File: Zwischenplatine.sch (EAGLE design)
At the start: 7 parts

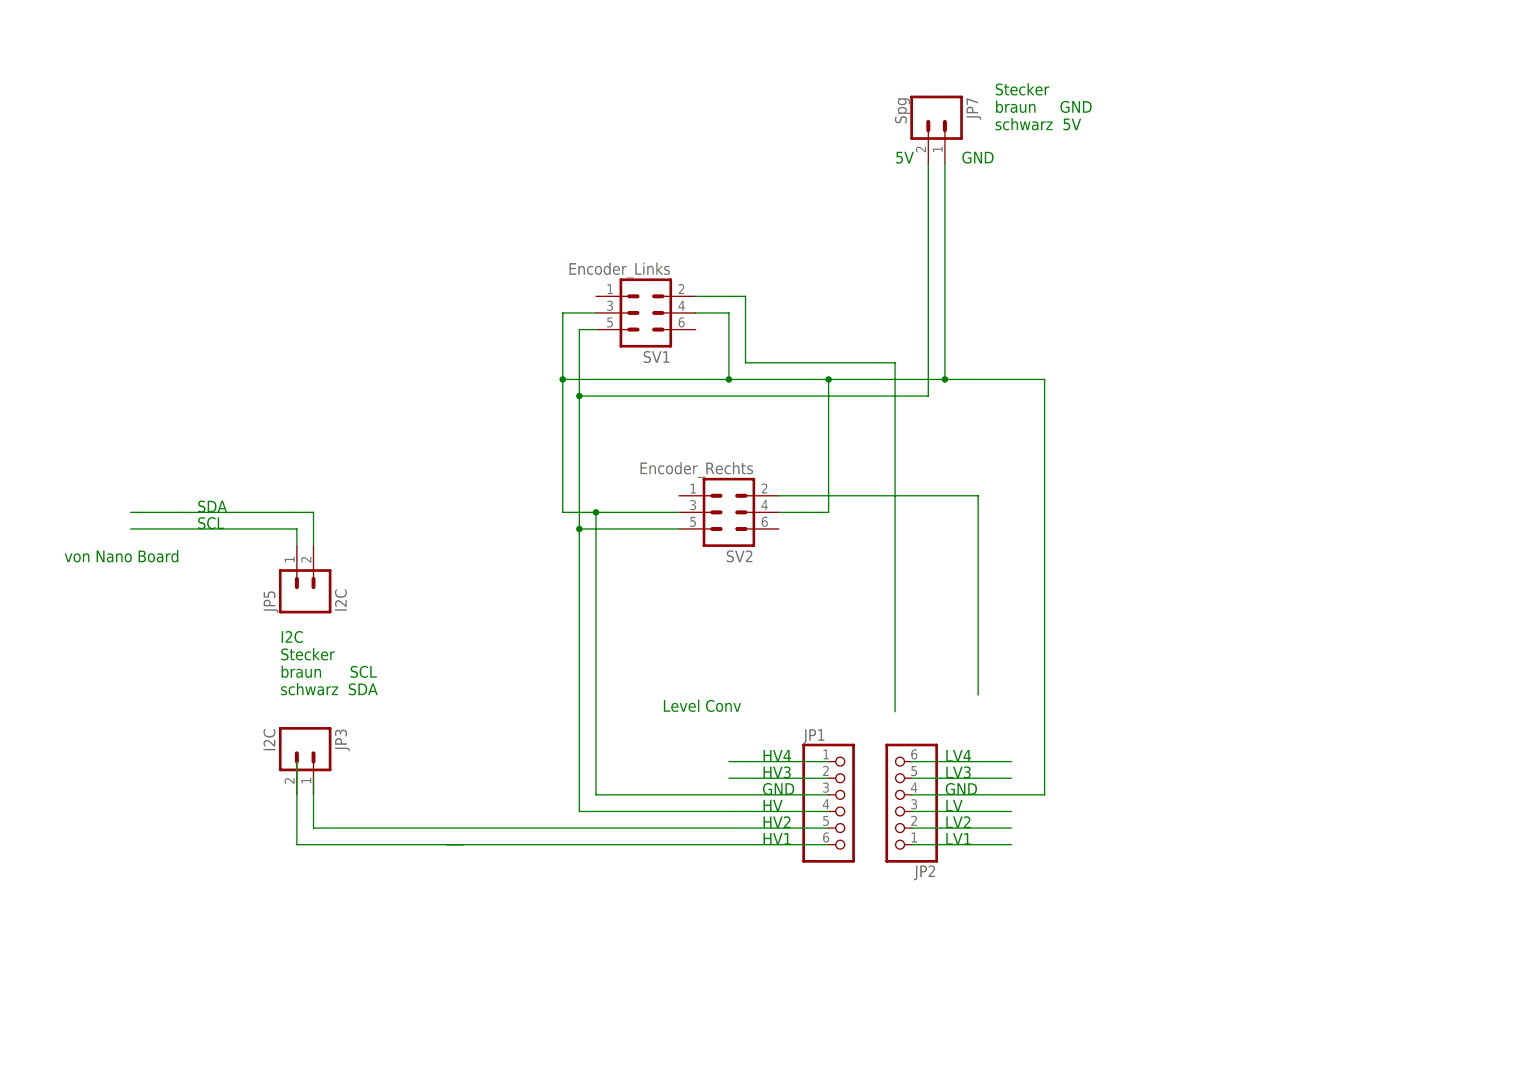
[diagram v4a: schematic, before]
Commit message: 
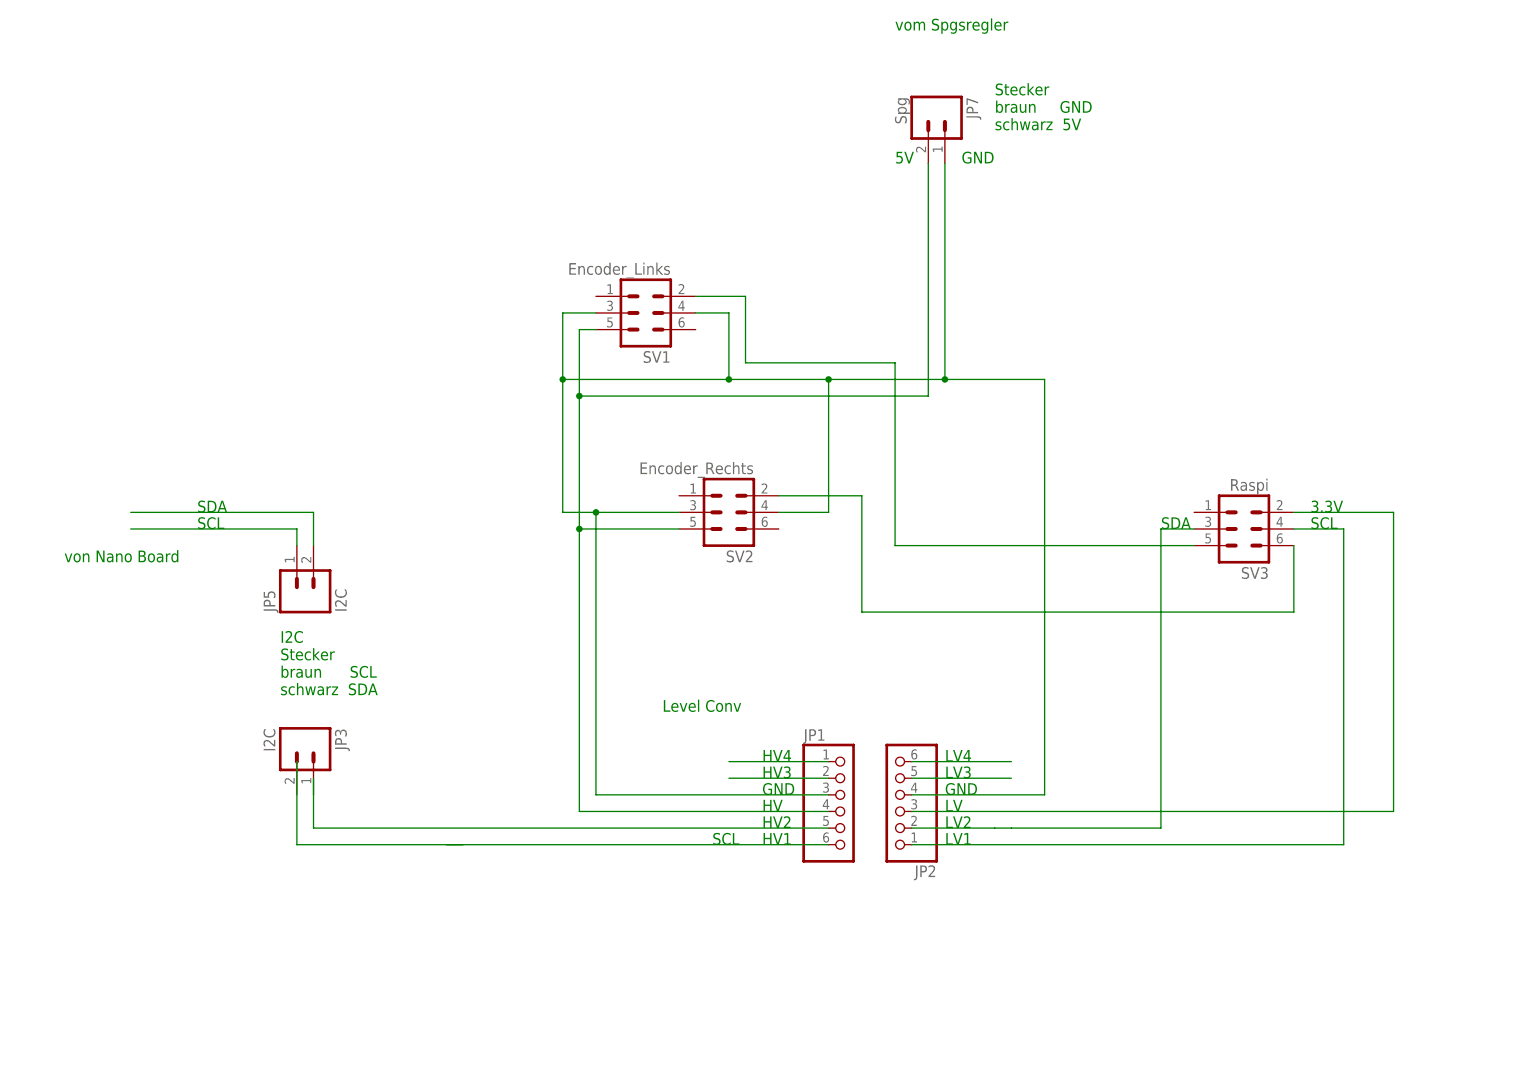
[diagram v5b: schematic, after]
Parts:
- added SV3: Raspi, con-ml:ML6
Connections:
- net N$12: now also SV3.2
- net N$13: now also SV3.3
- net N$14: now also SV3.4
- net PE4: now also SV3.5
- net PE5: now also SV3.6
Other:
- note added: "3.3V"
- note added: "vom Spgsregler"
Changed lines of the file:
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@@
 <part name="JP5" library="SparkFun-Connectors" deviceset="M02" device="-JST-2MM-SMT" value="I2C"/>
 <part name="JP3" library="SparkFun-Connectors" deviceset="M02" device="-JST-2MM-SMT" value="I2C"/>
+<part name="SV3" library="con-ml" deviceset="ML6" device="" value="Raspi"/>
 </parts>
 <sheets>
@@
 schwarz  SDA</text>
 <text x="-73.66" y="78.74" size="1.778" layer="91">von Nano Board</text>
+<text x="25.4" y="35.56" size="1.778" layer="91">SCL</text>
+<text x="116.84" y="83.82" size="1.778" layer="91">SCL</text>
+<text x="116.84" y="86.36" size="1.778" layer="91">3.3V</text>
+<text x="93.98" y="83.82" size="1.778" layer="91">SDA</text>
+<text x="53.34" y="160.02" size="1.778" layer="91">vom Spgsregler</text>
 </plain>
 <instances>
@@
 <instance part="JP5" gate="G$1" x="-35.56" y="73.66" rot="R90"/>
 <instance part="JP3" gate="G$1" x="-38.1" y="50.8" rot="R270"/>
+<instance part="SV3" gate="1" x="106.68" y="83.82" smashed="yes" rot="R180">
+<attribute name="VALUE" x="110.49" y="91.44" size="1.778" layer="96" rot="R180"/>
+<attribute name="NAME" x="110.49" y="77.978" size="1.778" layer="95" rot="R180"/>
+</instance>
 </instances>
 <busses>
@@
 <net name="PE5" class="0">
 <segment>
-<wire x1="35.56" y1="88.9" x2="66.04" y2="88.9" width="0.1524" layer="91"/>
-<wire x1="66.04" y1="88.9" x2="66.04" y2="58.42" width="0.1524" layer="91"/>
+<pinref part="SV3" gate="1" pin="6"/>
+<wire x1="114.3" y1="81.28" x2="114.3" y2="71.12" width="0.1524" layer="91"/>
+<wire x1="114.3" y1="71.12" x2="48.26" y2="71.12" width="0.1524" layer="91"/>
 <pinref part="SV2" gate="1" pin="2"/>
+<wire x1="35.56" y1="88.9" x2="48.26" y2="88.9" width="0.1524" layer="91"/>
+<wire x1="48.26" y1="88.9" x2="48.26" y2="71.12" width="0.1524" layer="91"/>
 </segment>
 </net>
@@
 <wire x1="30.48" y1="119.38" x2="30.48" y2="109.22" width="0.1524" layer="91"/>
 <wire x1="30.48" y1="109.22" x2="53.34" y2="109.22" width="0.1524" layer="91"/>
-<wire x1="53.34" y1="109.22" x2="53.34" y2="55.88" width="0.1524" layer="91"/>
+<wire x1="53.34" y1="109.22" x2="53.34" y2="81.28" width="0.1524" layer="91"/>
 <pinref part="SV1" gate="1" pin="2"/>
 <wire x1="30.48" y1="119.38" x2="22.86" y2="119.38" width="0.1524" layer="91"/>
+<pinref part="SV3" gate="1" pin="5"/>
+<wire x1="99.06" y1="81.28" x2="53.34" y2="81.28" width="0.1524" layer="91"/>
 </segment>
 </net>
@@
 <wire x1="5.08" y1="83.82" x2="5.08" y2="40.64" width="0.1524" layer="91"/>
 <pinref part="JP1" gate="A" pin="4"/>
-<wire x1="43.18" y1="40.64" x2="30.48" y2="40.64" width="0.1524" layer="91"/>
-<wire x1="30.48" y1="40.64" x2="27.94" y2="40.64" width="0.1524" layer="91"/>
-<wire x1="5.08" y1="40.64" x2="27.94" y2="40.64" width="0.1524" layer="91"/>
+<wire x1="5.08" y1="40.64" x2="43.18" y2="40.64" width="0.1524" layer="91"/>
 <junction x="5.08" y="83.82"/>
 </segment>
@@
 <segment>
 <pinref part="JP2" gate="A" pin="3"/>
-<wire x1="55.88" y1="40.64" x2="71.12" y2="40.64" width="0.1524" layer="91"/>
+<wire x1="55.88" y1="40.64" x2="129.54" y2="40.64" width="0.1524" layer="91"/>
+<wire x1="129.54" y1="40.64" x2="129.54" y2="86.36" width="0.1524" layer="91"/>
+<pinref part="SV3" gate="1" pin="2"/>
+<wire x1="129.54" y1="86.36" x2="114.3" y2="86.36" width="0.1524" layer="91"/>
 </segment>
 </net>
@@
 <segment>
 <pinref part="JP2" gate="A" pin="2"/>
-<wire x1="55.88" y1="38.1" x2="71.12" y2="38.1" width="0.1524" layer="91"/>
+<wire x1="55.88" y1="38.1" x2="68.58" y2="38.1" width="0.1524" layer="91"/>
+<pinref part="SV3" gate="1" pin="3"/>
+<wire x1="68.58" y1="38.1" x2="71.12" y2="38.1" width="0.1524" layer="91"/>
+<wire x1="99.06" y1="83.82" x2="93.98" y2="83.82" width="0.1524" layer="91"/>
+<wire x1="93.98" y1="83.82" x2="93.98" y2="38.1" width="0.1524" layer="91"/>
+<wire x1="93.98" y1="38.1" x2="71.12" y2="38.1" width="0.1524" layer="91"/>
 </segment>
 </net>
@@
 <segment>
 <pinref part="JP2" gate="A" pin="1"/>
-<wire x1="55.88" y1="35.56" x2="71.12" y2="35.56" width="0.1524" layer="91"/>
-</segment>
-</net>
+<wire x1="55.88" y1="35.56" x2="121.92" y2="35.56" width="0.1524" layer="91"/>
+<wire x1="121.92" y1="35.56" x2="121.92" y2="83.82" width="0.1524" layer="91"/>
+<pinref part="SV3" gate="1" pin="4"/>
+<wire x1="121.92" y1="83.82" x2="114.3" y2="83.82" width="0.1524" layer="91"/>
+</segment>
+</net>

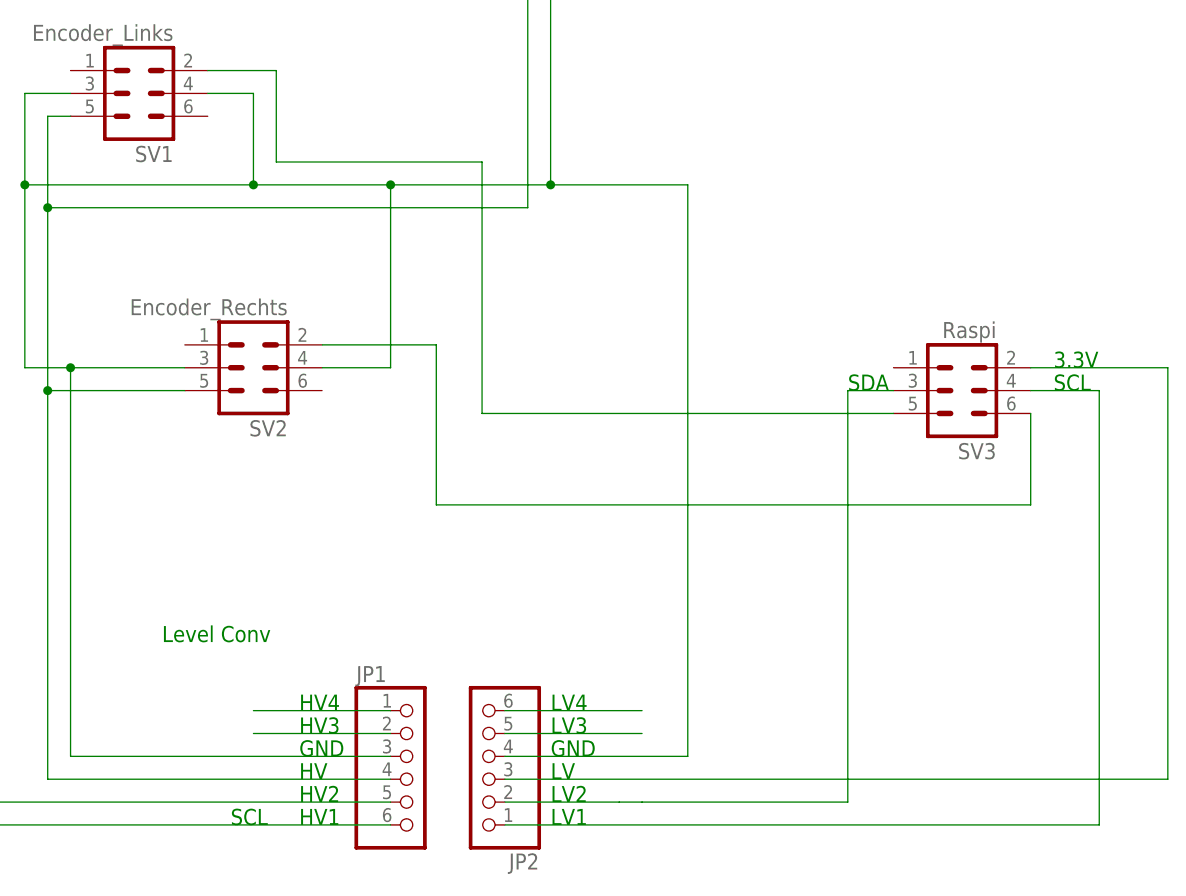
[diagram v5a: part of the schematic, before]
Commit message: 
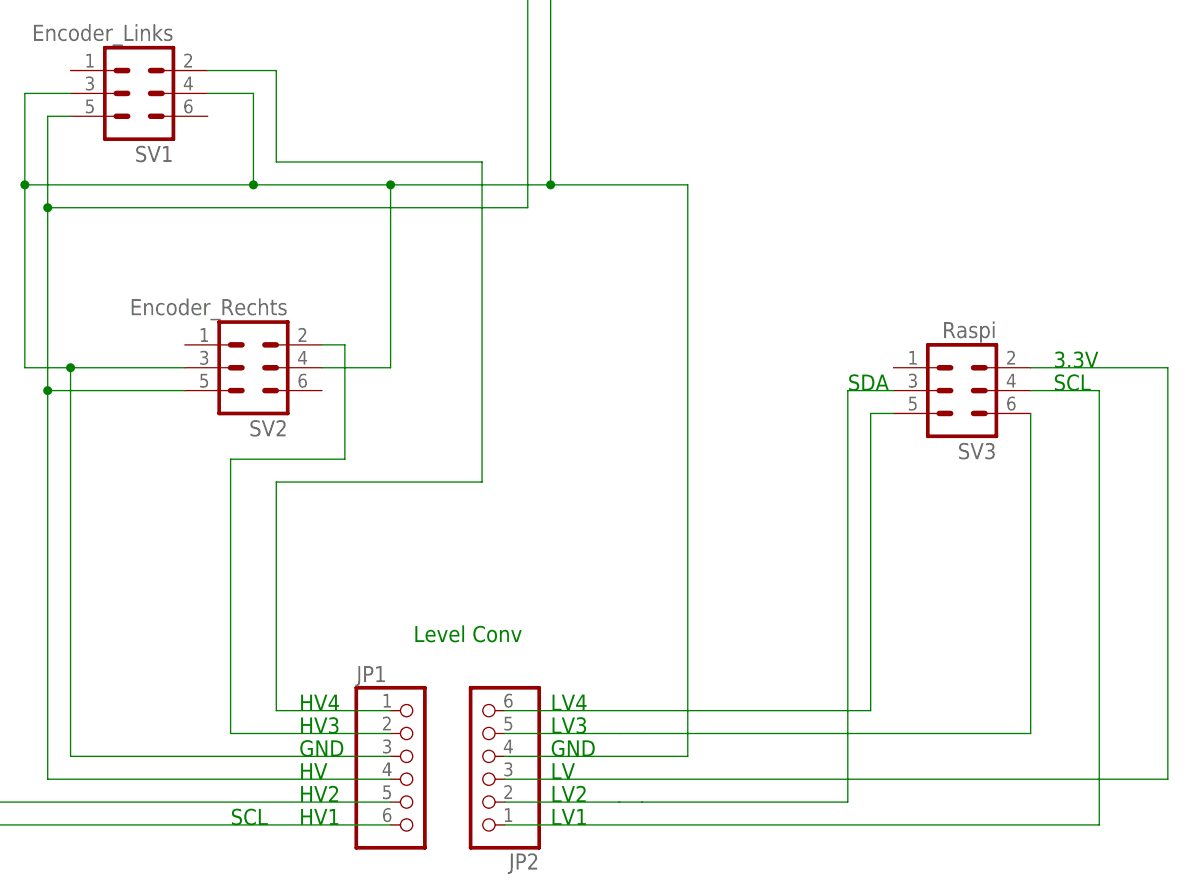
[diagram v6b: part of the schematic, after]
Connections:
- removed net N$3: JP1.1
- removed net N$4: JP1.2
- net N$10: now also SV3.6
- net N$9: now also SV3.5
- net PE4: now also JP1.1; no longer SV3.5
- net PE5: now also JP1.2; no longer SV3.6
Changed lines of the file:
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@@
 braun     GND
 schwarz  5V</text>
-<text x="17.78" y="55.88" size="1.778" layer="91">Level Conv</text>
+<text x="45.72" y="55.88" size="1.778" layer="91">Level Conv</text>
 <text x="33.02" y="35.56" size="1.778" layer="91">HV1</text>
 <text x="33.02" y="38.1" size="1.778" layer="91">HV2</text>
@@
 <net name="PE5" class="0">
 <segment>
-<pinref part="SV3" gate="1" pin="6"/>
-<wire x1="114.3" y1="81.28" x2="114.3" y2="71.12" width="0.1524" layer="91"/>
-<wire x1="114.3" y1="71.12" x2="48.26" y2="71.12" width="0.1524" layer="91"/>
 <pinref part="SV2" gate="1" pin="2"/>
-<wire x1="35.56" y1="88.9" x2="48.26" y2="88.9" width="0.1524" layer="91"/>
-<wire x1="48.26" y1="88.9" x2="48.26" y2="71.12" width="0.1524" layer="91"/>
+<wire x1="35.56" y1="88.9" x2="38.1" y2="88.9" width="0.1524" layer="91"/>
+<pinref part="JP1" gate="A" pin="2"/>
+<wire x1="43.18" y1="45.72" x2="25.4" y2="45.72" width="0.1524" layer="91"/>
+<wire x1="25.4" y1="45.72" x2="25.4" y2="76.2" width="0.1524" layer="91"/>
+<wire x1="25.4" y1="76.2" x2="38.1" y2="76.2" width="0.1524" layer="91"/>
+<wire x1="38.1" y1="76.2" x2="38.1" y2="88.9" width="0.1524" layer="91"/>
 </segment>
 </net>
@@
 <wire x1="30.48" y1="119.38" x2="30.48" y2="109.22" width="0.1524" layer="91"/>
 <wire x1="30.48" y1="109.22" x2="53.34" y2="109.22" width="0.1524" layer="91"/>
-<wire x1="53.34" y1="109.22" x2="53.34" y2="81.28" width="0.1524" layer="91"/>
+<wire x1="53.34" y1="109.22" x2="53.34" y2="73.66" width="0.1524" layer="91"/>
 <pinref part="SV1" gate="1" pin="2"/>
 <wire x1="30.48" y1="119.38" x2="22.86" y2="119.38" width="0.1524" layer="91"/>
-<pinref part="SV3" gate="1" pin="5"/>
-<wire x1="99.06" y1="81.28" x2="53.34" y2="81.28" width="0.1524" layer="91"/>
+<pinref part="JP1" gate="A" pin="1"/>
+<wire x1="43.18" y1="48.26" x2="30.48" y2="48.26" width="0.1524" layer="91"/>
+<wire x1="30.48" y1="48.26" x2="30.48" y2="73.66" width="0.1524" layer="91"/>
+<wire x1="30.48" y1="73.66" x2="53.34" y2="73.66" width="0.1524" layer="91"/>
 </segment>
 </net>
@@
 </segment>
 </net>
-<net name="N$3" class="0">
-<segment>
-<pinref part="JP1" gate="A" pin="1"/>
-<wire x1="43.18" y1="48.26" x2="27.94" y2="48.26" width="0.1524" layer="91"/>
-</segment>
-</net>
-<net name="N$4" class="0">
-<segment>
-<pinref part="JP1" gate="A" pin="2"/>
-<wire x1="43.18" y1="45.72" x2="27.94" y2="45.72" width="0.1524" layer="91"/>
-</segment>
-</net>
 <net name="N$7" class="0">
 <segment>
@@
 <segment>
 <pinref part="JP2" gate="A" pin="6"/>
-<wire x1="55.88" y1="48.26" x2="71.12" y2="48.26" width="0.1524" layer="91"/>
+<wire x1="55.88" y1="48.26" x2="96.52" y2="48.26" width="0.1524" layer="91"/>
+<wire x1="96.52" y1="48.26" x2="96.52" y2="81.28" width="0.1524" layer="91"/>
+<pinref part="SV3" gate="1" pin="5"/>
+<wire x1="96.52" y1="81.28" x2="99.06" y2="81.28" width="0.1524" layer="91"/>
 </segment>
 </net>
@@
 <segment>
 <pinref part="JP2" gate="A" pin="5"/>
-<wire x1="55.88" y1="45.72" x2="71.12" y2="45.72" width="0.1524" layer="91"/>
+<wire x1="55.88" y1="45.72" x2="68.58" y2="45.72" width="0.1524" layer="91"/>
+<pinref part="SV3" gate="1" pin="6"/>
+<wire x1="68.58" y1="45.72" x2="71.12" y2="45.72" width="0.1524" layer="91"/>
+<wire x1="71.12" y1="45.72" x2="114.3" y2="45.72" width="0.1524" layer="91"/>
+<wire x1="114.3" y1="45.72" x2="114.3" y2="81.28" width="0.1524" layer="91"/>
 </segment>
 </net>
